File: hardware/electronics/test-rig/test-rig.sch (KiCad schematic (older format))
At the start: 56 parts, among them IC1 23LC1024, J1 JUMPER_OPEN, J2 JUMPER_CLOSED, J3 JUMPER_CLOSED, J4 AudioJack3_Switch, J5 Screw_Terminal_1x02, J6 Screw_Terminal_1x02, P1 CONN_01X15, P2 CONN_01X15, P3 CONN_01X04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

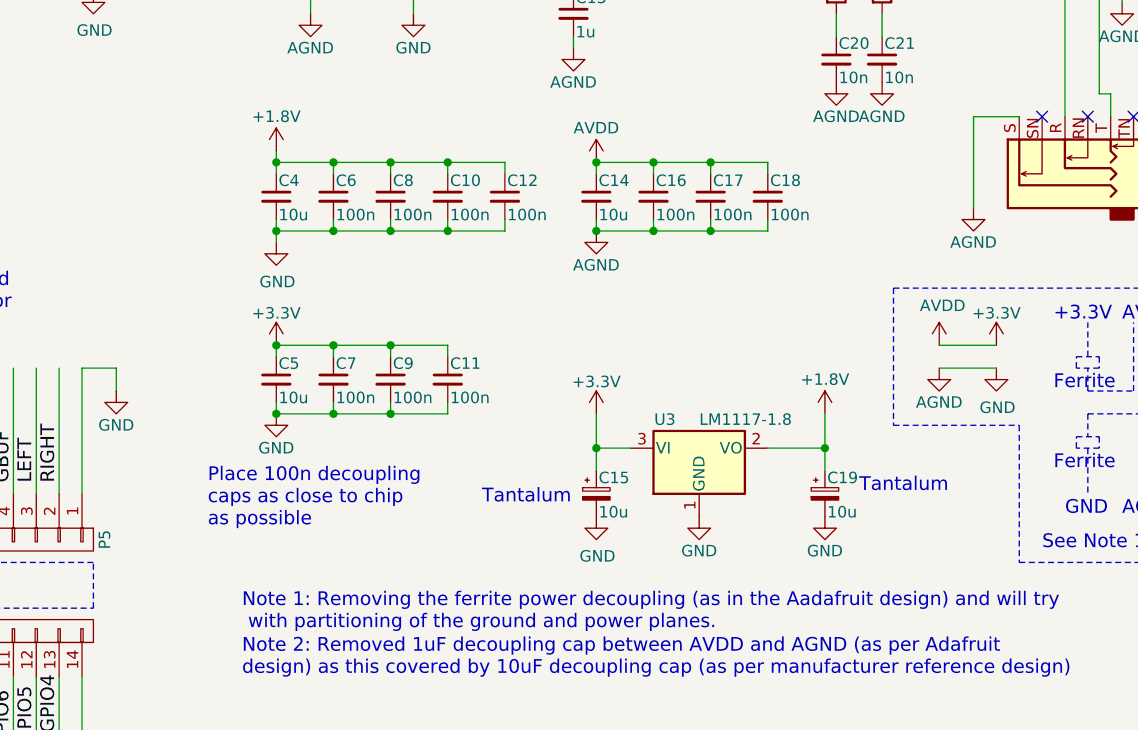
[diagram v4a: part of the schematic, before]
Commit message: Removed double 10u decoupling caps in VS1053 power supply
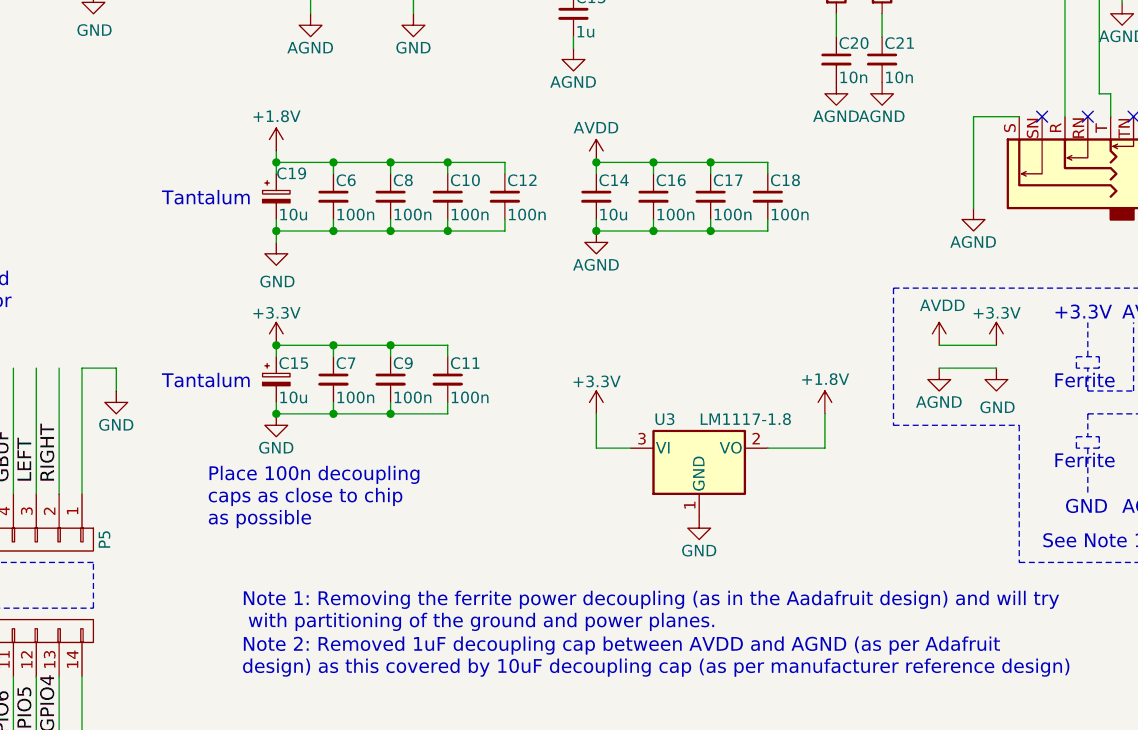
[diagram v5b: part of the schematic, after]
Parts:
- removed C4, C5: 10u, Capacitors_SMD:C_0805_HandSoldering, symbol modular-internet-radio:C_Small
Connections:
- wire segments 297 -> 295
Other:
- moved on the sheet: C15, C19
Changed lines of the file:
@@
 L modular-internet-radio:CP_Small C15
 U 1 1 5D7F3988
-P 8550 6150
-F 0 "C15" H 8560 6220 50  0000 L CNN
-F 1 "10u" H 8560 6070 50  0000 L CNN
-F 2 "Capacitors_Tantalum_SMD:CP_Tantalum_Case-D_EIA-7343-31_Hand" H 8550 6150 50  0001 C CNN
-F 3 "" H 8550 6150 50  0000 C CNN
-	1    8550 6150
+P 7150 5650
+F 0 "C15" H 7160 5720 50  0000 L CNN
+F 1 "10u" H 7160 5570 50  0000 L CNN
+F 2 "Capacitors_Tantalum_SMD:CP_Tantalum_Case-D_EIA-7343-31_Hand" H 7150 5650 50  0001 C CNN
+F 3 "" H 7150 5650 50  0000 C CNN
+	1    7150 5650
 	1    0    0    -1
 $EndComp
@@
 L modular-internet-radio:CP_Small C19
 U 1 1 5D7F3A2C
-P 9550 6150
-F 0 "C19" H 9560 6220 50  0000 L CNN
-F 1 "10u" H 9560 6070 50  0000 L CNN
-F 2 "Capacitors_Tantalum_SMD:CP_Tantalum_Case-D_EIA-7343-31_Hand" H 9550 6150 50  0001 C CNN
-F 3 "" H 9550 6150 50  0000 C CNN
-	1    9550 6150
-	1    0    0    -1
-$EndComp
-$Comp
-L modular-internet-radio:GND #PWR038
-U 1 1 5D7F3C90
-P 9550 6250
-F 0 "#PWR038" H 9550 6000 50  0001 C CNN
-F 1 "GND" H 9550 6100 50  0000 C CNN
-F 2 "" H 9550 6250 50  0000 C CNN
-F 3 "" H 9550 6250 50  0000 C CNN
-	1    9550 6250
-	1    0    0    -1
-$EndComp
-Text Notes 8050 6200 0    60   ~ 0
+P 7150 4850
+F 0 "C19" H 7150 4950 50  0000 L CNN
+F 1 "10u" H 7160 4770 50  0000 L CNN
+F 2 "Capacitors_Tantalum_SMD:CP_Tantalum_Case-D_EIA-7343-31_Hand" H 7150 4850 50  0001 C CNN
+F 3 "" H 7150 4850 50  0000 C CNN
+	1    7150 4850
+	1    0    0    -1
+$EndComp
+Text Notes 6650 5700 0    60   ~ 0
 Tantalum
-Text Notes 9700 6150 0    60   ~ 0
+Text Notes 6650 4900 0    60   ~ 0
 Tantalum
 $Comp
@@
 Wire Wire Line
 	8550 5800 8550 5950
-Connection ~ 8550 5950
-Connection ~ 9550 5950
 Wire Wire Line
 	10650 1000 10650 1050
@@
 	8100 1650 8100 1700
 Wire Wire Line
-	8550 5950 8550 6050
-Wire Wire Line
-	9550 5950 9550 6050
-Wire Wire Line
 	7300 3950 7300 4050
 Wire Wire Line
@@
 F 3 "" H 7150 5050 50  0000 C CNN
 	1    7150 5050
-	1    0    0    -1
-$EndComp
-$Comp
-L modular-internet-radio:GND #PWR033
-U 1 1 5DA4FBB4
-P 8550 6250
-F 0 "#PWR033" H 8550 6000 50  0001 C CNN
-F 1 "GND" H 8555 6077 50  0000 C CNN
-F 2 "" H 8550 6250 50  0000 C CNN
-F 3 "" H 8550 6250 50  0000 C CNN
-	1    8550 6250
 	1    0    0    -1
 $EndComp
@@
 Connection ~ 1550 5350
 $Comp
-L modular-internet-radio:C_Small C4
-U 1 1 5DA3BCB8
-P 7150 4850
-F 0 "C4" H 7160 4920 50  0000 L CNN
-F 1 "10u" H 7160 4770 50  0000 L CNN
-F 2 "Capacitors_SMD:C_0805_HandSoldering" H 7150 4850 50  0001 C CNN
-F 3 "" H 7150 4850 50  0000 C CNN
-	1    7150 4850
-	1    0    0    -1
-$EndComp
-$Comp
-L modular-internet-radio:C_Small C5
-U 1 1 5DA3C160
-P 7150 5650
-F 0 "C5" H 7160 5720 50  0000 L CNN
-F 1 "10u" H 7160 5570 50  0000 L CNN
-F 2 "Capacitors_SMD:C_0805_HandSoldering" H 7150 5650 50  0001 C CNN
-F 3 "" H 7150 5650 50  0000 C CNN
-	1    7150 5650
-	1    0    0    -1
-$EndComp
-$Comp
 L modular-internet-radio:C_Small C14

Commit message: New schematic
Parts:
- removed P7: CONN_01X01, Pin_Headers:Pin_Header_Straight_1x01_Pitch2.54mm, symbol modular-internet-radio:CONN_01X01
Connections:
- net labels removed: VCO
- wire segments 295 -> 292
- no-connect marks 10 -> 12
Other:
- note removed: "Ground pin for \noscilloscope"
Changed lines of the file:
@@
 Text Label 9200 3150 0    60   ~ 0
 RX
-Text Notes 4950 5350 0    60   ~ 0
+Text Notes 5350 5250 0    60   ~ 0
 Unused GPIO pins should \nhave a pull-down resistor
-Text Notes 10950 1250 1    60   ~ 0
-Ground pin for \noscilloscope
 $Comp
 L modular-internet-radio:R R13
@@
 F 3 "" H 6350 3850 50  0000 C CNN
 	1    6350 3850
-	1    0    0    -1
-$EndComp
-$Comp
-L modular-internet-radio:CONN_01X01 P7
-U 1 1 5D7FC3E1
-P 10650 800
-F 0 "P7" H 10650 900 50  0000 C CNN
-F 1 "CONN_01X01" V 10750 800 50  0001 C CNN
-F 2 "Pin_Headers:Pin_Header_Straight_1x01_Pitch2.54mm" H 10650 800 50  0001 C CNN
-F 3 "" H 10650 800 50  0000 C CNN
-	1    10650 800
-	0    -1   -1   0
-$EndComp
-$Comp
-L modular-internet-radio:GND #PWR047
-U 1 1 5D7FC49C
-P 10650 1050
-F 0 "#PWR047" H 10650 800 50  0001 C CNN
-F 1 "GND" H 10650 900 50  0000 C CNN
-F 2 "" H 10650 1050 50  0000 C CNN
-F 3 "" H 10650 1050 50  0000 C CNN
-	1    10650 1050
 	1    0    0    -1
 $EndComp
@@
 Text Notes 4750 600  0    60   ~ 0
 MP3 CODEC
-Text Label 6550 3150 0    60   ~ 0
-VCO
 Text Label 8900 3300 0    60   ~ 0
 GBUF
@@
 L modular-internet-radio:+3.3V #PWR013
 U 1 1 5D84F935
-P 4850 5850
-F 0 "#PWR013" H 4850 5700 50  0001 C CNN
-F 1 "+3.3V" H 4850 5990 50  0000 C CNN
-F 2 "" H 4850 5850 50  0000 C CNN
-F 3 "" H 4850 5850 50  0000 C CNN
-	1    4850 5850
-	1    0    0    -1
-$EndComp
-Text Label 5100 6950 3    60   ~ 0
+P 5600 7500
+F 0 "#PWR013" H 5600 7350 50  0001 C CNN
+F 1 "+3.3V" H 5600 7650 50  0000 C CNN
+F 2 "" H 5600 7500 50  0000 C CNN
+F 3 "" H 5600 7500 50  0000 C CNN
+	1    5600 7500
+	-1   0    0    1
+$EndComp
+Text Label 5800 7000 3    60   ~ 0
 XDCS/IO27
-Text Label 5200 6950 3    60   ~ 0
+Text Label 5100 7000 3    60   ~ 0
 DREQ/IO26
-Text Label 5300 7000 3    60   ~ 0
+Text Label 6000 7050 3    60   ~ 0
 XCS/IO25
-Text Label 5400 7450 1    60   ~ 0
+Text Label 5300 6100 1    60   ~ 0
 SO/IO19
-Text Label 5500 7100 3    60   ~ 0
+Text Label 5400 5750 3    60   ~ 0
 SI/IO23
-Text Label 5100 6100 1    60   ~ 0
+Text Label 5000 7500 1    60   ~ 0
 MP3RST
-Text Label 5600 6100 1    60   ~ 0
-VCO
 Text Label 5700 6100 1    60   ~ 0
 MICN
+Text Label 5800 6100 1    60   ~ 0
+MICP/LINE1
 Text Label 5900 6100 1    60   ~ 0
-MICP/LINE1
-Text Label 5800 6100 1    60   ~ 0
 LINE2
-Text Label 5800 7450 1    60   ~ 0
+Text Label 5500 6100 1    60   ~ 0
 SCK/IO18
-Text Label 6200 7500 1    60   ~ 0
+Text Label 5000 6150 1    60   ~ 0
 LROUT/GPIO4
 Text Label 6100 7500 1    60   ~ 0
 MCLK/GPIO5
-Text Label 5900 7500 1    60   ~ 0
+Text Label 5500 7500 1    60   ~ 0
 SDATA/GPIO7
 Text Label 5200 6100 1    60   ~ 0
 GPIO0
-Text Label 5300 6100 1    60   ~ 0
+Text Label 5100 6100 1    60   ~ 0
 GPIO1
-Text Label 5400 6100 1    60   ~ 0
+Text Label 5200 7500 1    60   ~ 0
 GPIO2
-Text Label 5500 6100 1    60   ~ 0
+Text Label 5300 7500 1    60   ~ 0
 GPIO3
+Text Label 6100 6100 1    60   ~ 0
+GBUF
 Text Label 6000 6100 1    60   ~ 0
-GBUF
-Text Label 6100 6100 1    60   ~ 0
 LEFT
 Text Label 6200 6100 1    60   ~ 0
 RIGHT
-Text Label 5600 7450 1    60   ~ 0
+Text Label 6300 7500 1    60   ~ 0
 TX
-Text Label 5700 7450 1    60   ~ 0
+Text Label 6200 7500 1    60   ~ 0
 RX
-Text Label 6000 7500 1    60   ~ 0
+Text Label 5400 7500 1    60   ~ 0
 SCLK/GPIO6
 $Comp
 L modular-internet-radio:GND #PWR017
 U 1 1 5D856EAE
-P 6300 7500
-F 0 "#PWR017" H 6300 7250 50  0001 C CNN
-F 1 "GND" H 6300 7350 50  0000 C CNN
-F 2 "" H 6300 7500 50  0000 C CNN
-F 3 "" H 6300 7500 50  0000 C CNN
-	1    6300 7500
+P 5800 7600
+F 0 "#PWR017" H 5800 7350 50  0001 C CNN
+F 1 "GND" H 5800 7450 50  0000 C CNN
+F 2 "" H 5800 7600 50  0000 C CNN
+F 3 "" H 5800 7600 50  0000 C CNN
+	1    5800 7600
 	1    0    0    -1
 $EndComp
@@
 	8550 5800 8550 5950
 Wire Wire Line
-	10650 1000 10650 1050
-Wire Wire Line
 	7300 3850 7300 3950
 Wire Wire Line
@@
 	4550 7800 4550 450
 Wire Wire Line
-	6900 3150 6400 3150
-Wire Wire Line
 	8800 3300 9350 3300
 Wire Notes Line
@@
 	6350 6450 4950 6450
 Wire Wire Line
-	5000 6150 5000 5850
+	5000 6150 5000 5600
 Wire Wire Line
 	5100 6150 5100 5600
@@
 	5500 6150 5500 5600
 Wire Wire Line
-	5600 6150 5600 5600
-Wire Wire Line
-	5700 6150 5700 5600
-Wire Wire Line
 	5800 6150 5800 5600
 Wire Wire Line
@@
 	6200 6150 6200 5600
 Wire Wire Line
-	6300 6150 6300 5600
-Wire Wire Line
 	5000 6950 5000 7500
 Wire Wire Line
@@
 	5600 6950 5600 7500
 Wire Wire Line
-	5700 6950 5700 7500
-Wire Wire Line
 	5800 6950 5800 7500
 Wire Wire Line
-	5900 6950 5900 7500
+	5900 6950 5900 7550
 Wire Wire Line
 	6000 6950 6000 7500
@@
 Wire Wire Line
 	6300 6950 6300 7500
-Wire Wire Line
-	5000 5850 4850 5850
 Wire Wire Line
 	9900 3500 9900 3700
@@
 	6000 6150 6000 5600
 $Comp
-L modular-internet-radio:+3.3V #PWR0103
-U 1 1 5DAF44E9
-P 4850 7400
-F 0 "#PWR0103" H 4850 7250 50  0001 C CNN
-F 1 "+3.3V" H 4850 7550 50  0000 C CNN
-F 2 "" H 4850 7400 50  0000 C CNN
-F 3 "" H 4850 7400 50  0000 C CNN
-	1    4850 7400
-	1    0    0    -1
-$EndComp
-Wire Wire Line
-	4850 7400 4850 7500
-Wire Wire Line
-	4850 7500 5000 7500
-$Comp
 L modular-internet-radio:GND #PWR0104
 U 1 1 5DB0D1A5
-P 6450 5700
-F 0 "#PWR0104" H 6450 5450 50  0001 C CNN
-F 1 "GND" H 6450 5550 50  0000 C CNN
-F 2 "" H 6450 5700 50  0000 C CNN
-F 3 "" H 6450 5700 50  0000 C CNN
-	1    6450 5700
-	1    0    0    -1
-$EndComp
-Wire Wire Line
-	6300 5600 6450 5600
-Wire Wire Line
-	6450 5600 6450 5700
+P 6450 5350
+F 0 "#PWR0104" H 6450 5100 50  0001 C CNN
+F 1 "GND" H 6450 5200 50  0000 C CNN
+F 2 "" H 6450 5350 50  0000 C CNN
+F 3 "" H 6450 5350 50  0000 C CNN
+	1    6450 5350
+	1    0    0    -1
+$EndComp
 $Comp
 L Connector:AudioJack3_Switch J4
@@
 	1    0    0    -1
 $EndComp
+Wire Wire Line
+	5700 5600 5700 6150
+$Comp
+L modular-internet-radio:+3.3V #PWR0101
+U 1 1 5DCB868F
+P 5550 5450
+F 0 "#PWR0101" H 5550 5300 50  0001 C CNN
+F 1 "+3.3V" H 5550 5600 50  0000 C CNN
+F 2 "" H 5550 5450 50  0000 C CNN
+F 3 "" H 5550 5450 50  0000 C CNN
+	1    5550 5450
+	1    0    0    -1
+$EndComp
+Wire Wire Line
+	5700 7600 5800 7600
+Wire Wire Line
+	5700 6950 5700 7600
+Wire Wire Line
+	5600 5500 5550 5500
+Wire Wire Line
+	5550 5500 5550 5450
+Wire Wire Line
+	5600 5500 5600 6150
+Wire Wire Line
+	6300 5350 6450 5350
+Wire Wire Line
+	6300 5350 6300 6150
+NoConn ~ 6900 3150
+NoConn ~ 5900 7550
 $EndSCHEMATC
